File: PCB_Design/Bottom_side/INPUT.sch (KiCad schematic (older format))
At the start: 2 parts

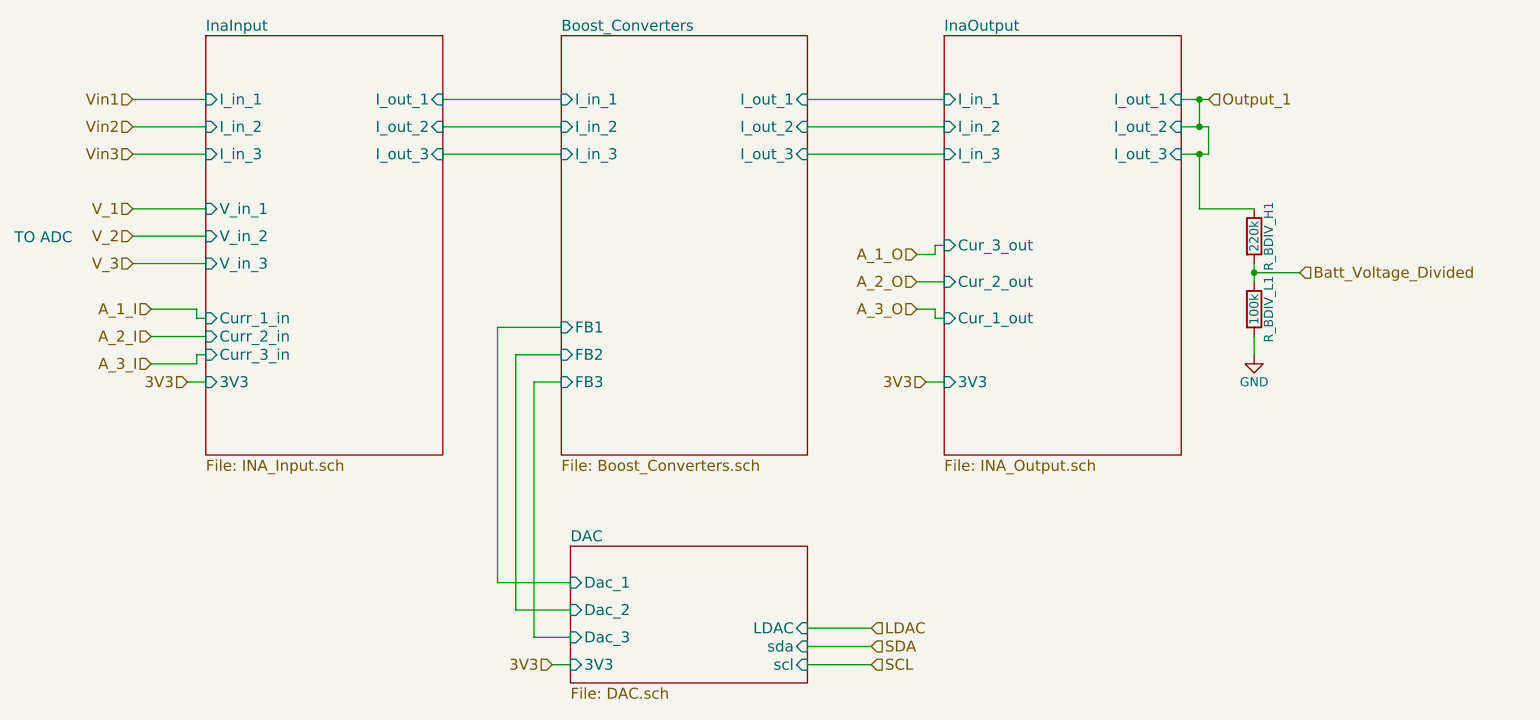
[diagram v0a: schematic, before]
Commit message: PCB bottom layer populated
PCB bottom layer populated, and waiting for top layer to be merged.
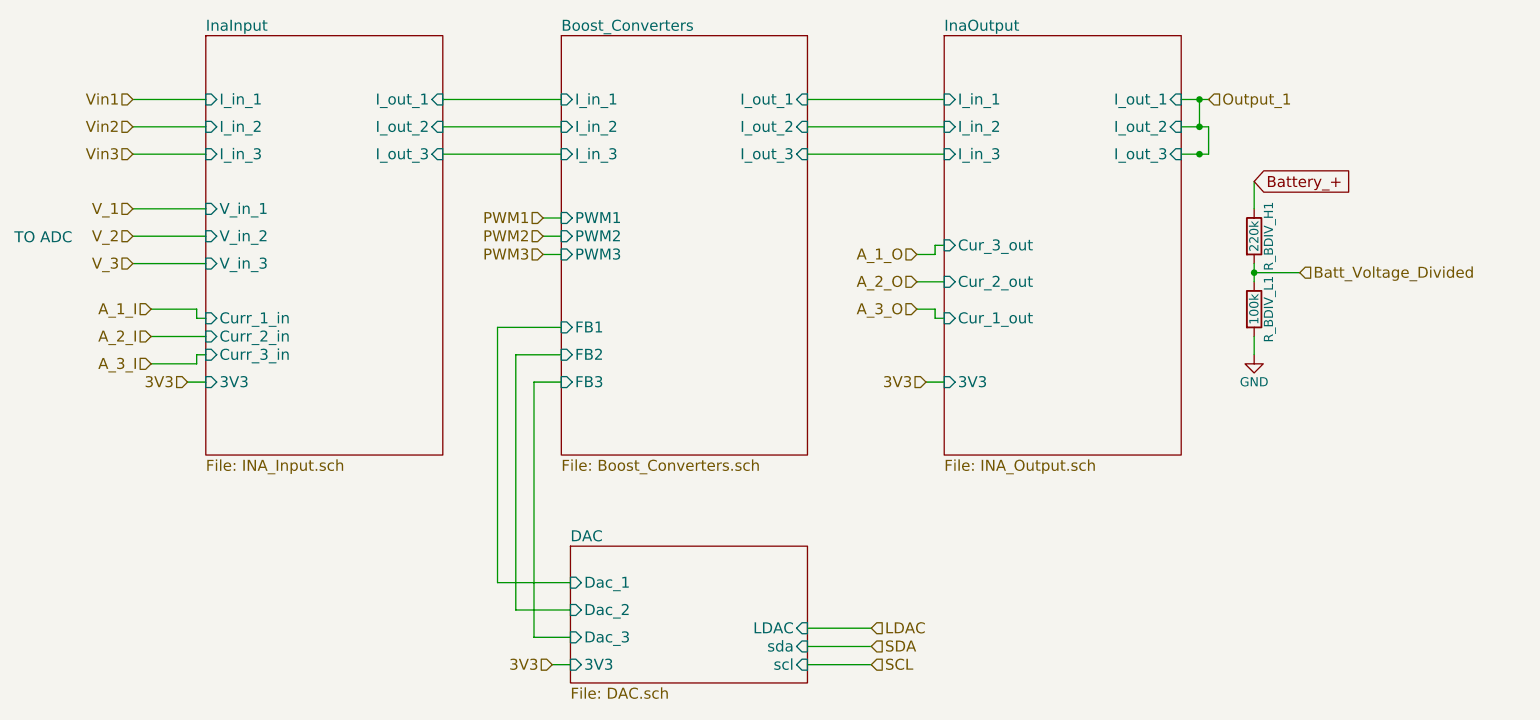
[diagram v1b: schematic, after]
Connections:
- net Output_1: no longer R_BDIV_H1.1
- new net Battery_+: R_BDIV_H1.1
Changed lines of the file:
@@
 LIBS:contrib
 LIBS:valves
-LIBS:Custom_Library
 LIBS:Bottom_side-cache
 EELAYER 25 0
@@
 $Descr A4 11693 8268
 encoding utf-8
-Sheet 2 25
+Sheet 2 26
 Title ""
 Date ""
@@
 F9 "I_out_2" I R 5250 2150 60
 F10 "I_out_3" I R 5250 2300 60
+F11 "PWM1" I L 3900 2650 60
+F12 "PWM2" I L 3900 2750 60
+F13 "PWM3" I L 3900 2850 60
 $EndSheet
 $Sheet
@@
 Wire Wire Line
 	3850 5100 3950 5100
-Wire Wire Line
-	7400 2300 7400 2600
 Connection ~ 7400 2300
-Wire Wire Line
-	7400 2600 7700 2600
 Wire Wire Line
 	7700 3300 7700 3400
@@
 Connection ~ 7400 2000
 Connection ~ 7400 2150
+Text GLabel 7700 2450 2    60   Input ~ 0
+Battery_+
+Wire Wire Line
+	7700 2450 7700 2600
+Text HLabel 3800 2650 0    60   Input ~ 0
+PWM1
+Wire Wire Line
+	3800 2650 3900 2650
+Text HLabel 3800 2750 0    60   Input ~ 0
+PWM2
+Text HLabel 3800 2850 0    60   Input ~ 0
+PWM3
+Wire Wire Line
+	3800 2750 3900 2750
+Wire Wire Line
+	3900 2850 3800 2850
 $EndSCHEMATC

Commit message: Updated PCB structure tree
Full_PCB now includes bottom and top layer hierarchical sheets
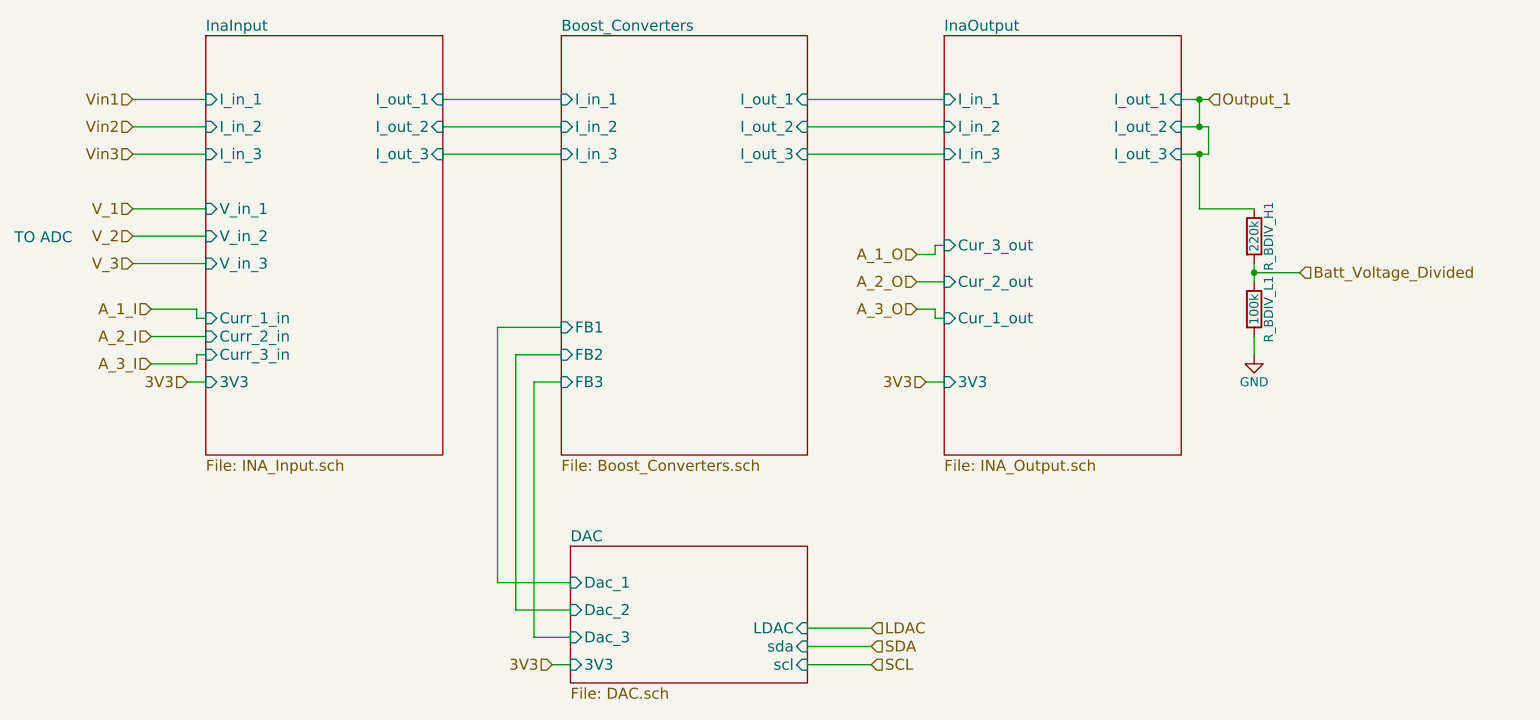
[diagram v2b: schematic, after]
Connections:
- net Battery_+ is gone; now on net Output_1: R_BDIV_H1.1
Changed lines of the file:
@@
 LIBS:power
 LIBS:device
-LIBS:switches
-LIBS:relays
-LIBS:motors
 LIBS:transistors
 LIBS:conn
@@
 LIBS:contrib
 LIBS:valves
-LIBS:Bottom_side-cache
+LIBS:Full_PCB-cache
 EELAYER 25 0
 EELAYER END
 $Descr A4 11693 8268
 encoding utf-8
-Sheet 2 26
+Sheet 3 26
 Title ""
 Date ""
@@
 F9 "I_out_2" I R 5250 2150 60
 F10 "I_out_3" I R 5250 2300 60
-F11 "PWM1" I L 3900 2650 60
-F12 "PWM2" I L 3900 2750 60
-F13 "PWM3" I L 3900 2850 60
 $EndSheet
 $Sheet
@@
 U 1 1 5A5EF949
 P 7700 2750
+AR Path="/5A57B48D/5A5EF949" Ref="R_BDIV_H1"  Part="1"
+AR Path="/5A799B71/5A77D148/5A5EF949" Ref="R_BDIV_H1"  Part="1"
 F 0 "R_BDIV_H1" V 7780 2750 50  0000 C CNN
 F 1 "220k" V 7700 2750 50  0000 C CNN
@@
 U 1 1 5A5EFA6C
 P 7700 3150
+AR Path="/5A57B48D/5A5EFA6C" Ref="R_BDIV_L1"  Part="1"
+AR Path="/5A799B71/5A77D148/5A5EFA6C" Ref="R_BDIV_L1"  Part="1"
 F 0 "R_BDIV_L1" V 7780 3150 50  0000 C CNN
 F 1 "100k" V 7700 3150 50  0000 C CNN
@@
 U 1 1 5A5EFD29
 P 7700 3400
+AR Path="/5A57B48D/5A5EFD29" Ref="#PWR01"  Part="1"
+AR Path="/5A799B71/5A77D148/5A5EFD29" Ref="#PWR01"  Part="1"
 F 0 "#PWR01" H 7700 3150 50  0001 C CNN
 F 1 "GND" H 7700 3250 50  0000 C CNN
@@
 Wire Wire Line
 	3850 5100 3950 5100
+Wire Wire Line
+	7400 2300 7400 2600
 Connection ~ 7400 2300
+Wire Wire Line
+	7400 2600 7700 2600
 Wire Wire Line
 	7700 3300 7700 3400
@@
 Connection ~ 7400 2000
 Connection ~ 7400 2150
-Text GLabel 7700 2450 2    60   Input ~ 0
-Battery_+
-Wire Wire Line
-	7700 2450 7700 2600
-Text HLabel 3800 2650 0    60   Input ~ 0
-PWM1
-Wire Wire Line
-	3800 2650 3900 2650
-Text HLabel 3800 2750 0    60   Input ~ 0
-PWM2
-Text HLabel 3800 2850 0    60   Input ~ 0
-PWM3
-Wire Wire Line
-	3800 2750 3900 2750
-Wire Wire Line
-	3900 2850 3800 2850
 $EndSCHEMATC
